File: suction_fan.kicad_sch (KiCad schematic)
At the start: 4 parts, among them U5_1 DRV8835DSSR

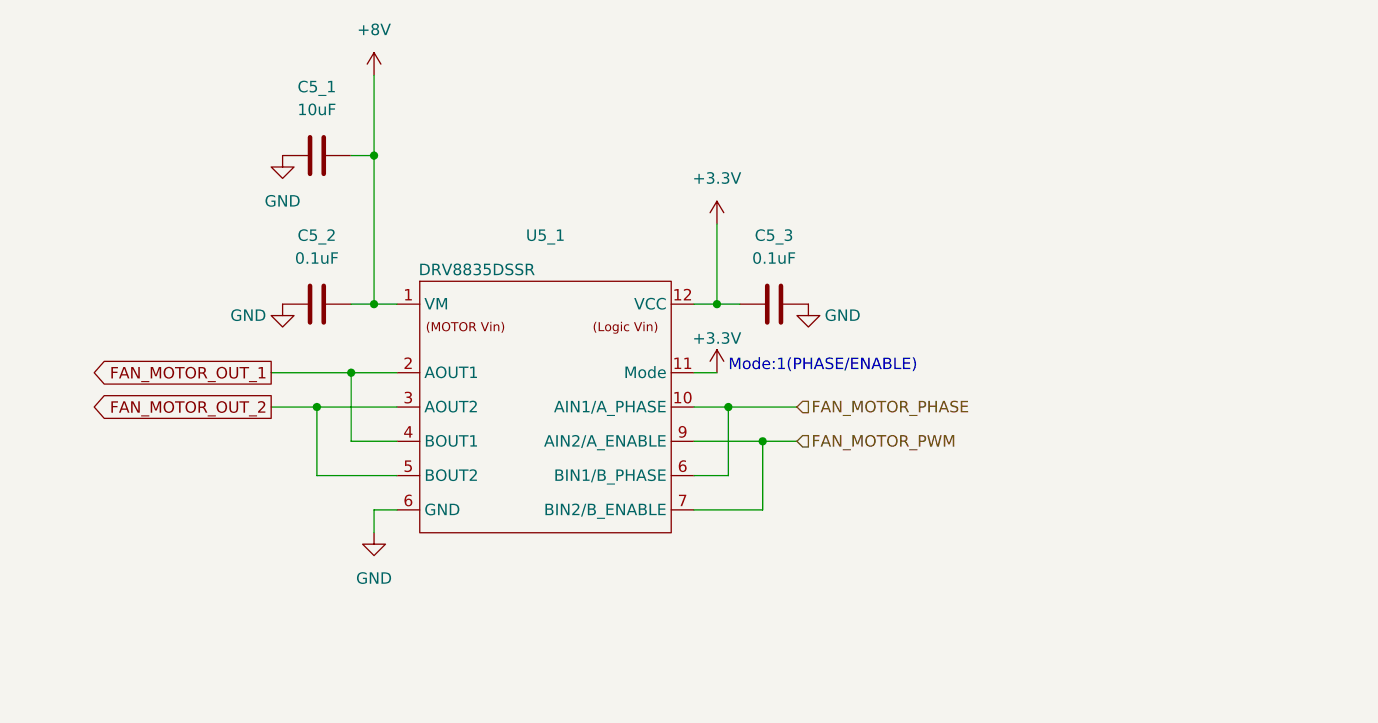
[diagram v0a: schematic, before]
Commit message: 吸引ファンモータのコネクタを追加
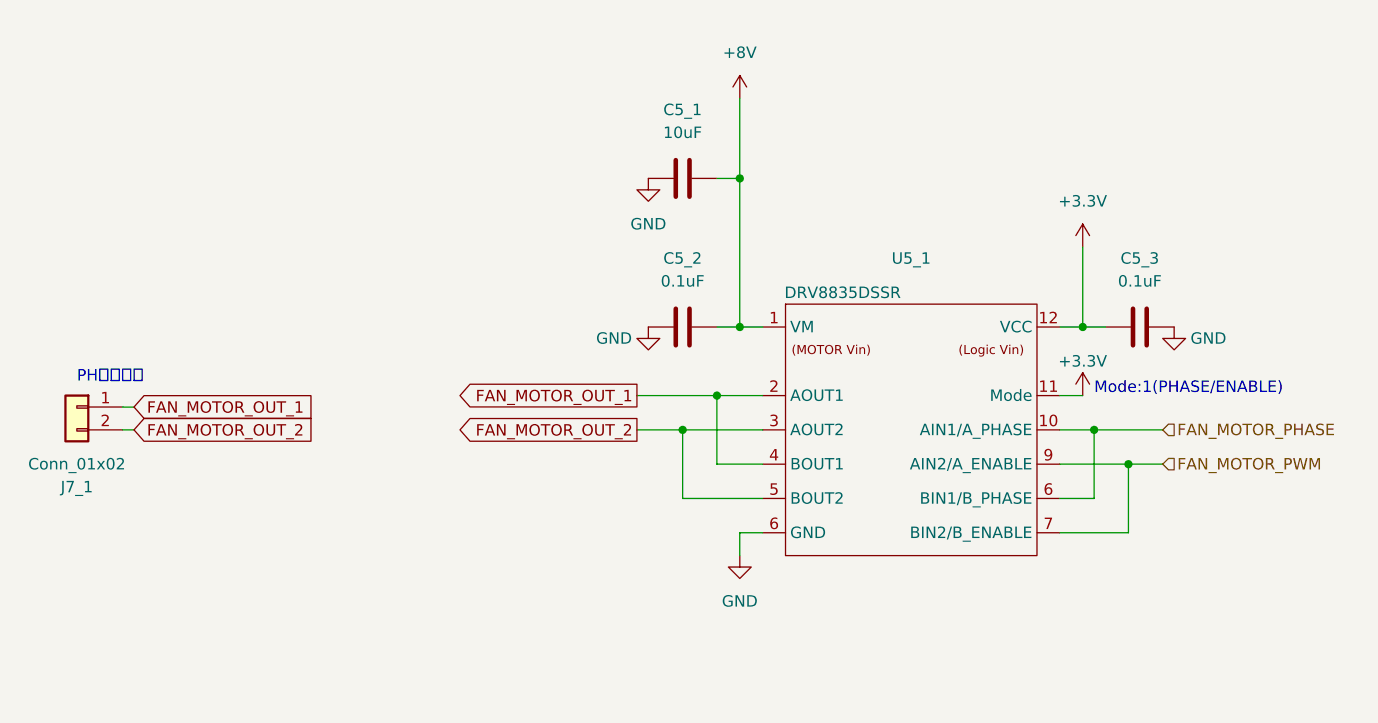
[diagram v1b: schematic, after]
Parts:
- added J7_1: Conn_01x02, symbol Connector_Generic:Conn_01x02
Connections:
- net FAN_MOTOR_OUT_1: now also J7_1.1 (Pin_1)
- net FAN_MOTOR_OUT_2: now also J7_1.2 (Pin_2)
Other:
- note added: "PHコネクタ"
- moved on the sheet: C5_1, C5_2, C5_3, U5_1

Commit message: 吸引モータ周りの回路修正
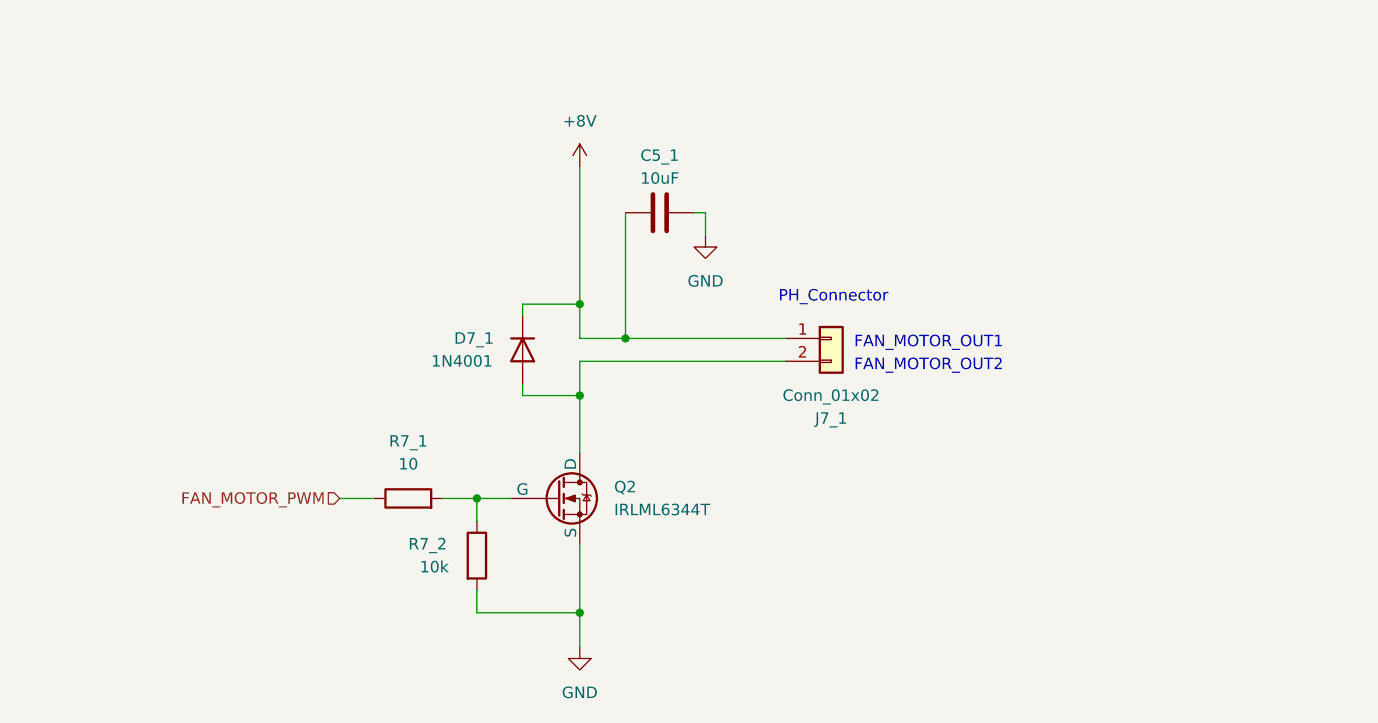
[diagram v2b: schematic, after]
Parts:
- removed C5_2, C5_3: 0.1uF, Capacitor_SMD:C_0603_1608Metric_Pad1.08x0.95mm_HandSolder, symbol Device:C
- removed U5_1: DRV8835DSSR, Self-Made_Generic_Packages:WSON-12-1EP_ExpandPad_3x2mm_P0.5mm_EP1x2.65, symbol DRV8835:DRV8835
- added D7_1: 1N4001, Diode_THT:D_DO-41_SOD81_P10.16mm_Horizontal, symbol Diode:1N4001
- added Q2: IRLML6344T, Package_TO_SOT_SMD:SOT-23, symbol Simulation_SPICE:NMOS
- added R7_1: 10, symbol Device:R
- added R7_2: 10k, symbol Device:R
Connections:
- net FAN_MOTOR_OUT_1 is gone; now on net +8V: J7_1.1 (Pin_1)
- net +8V: now also C5_1.1, D7_1.1 (K); no longer C5_1.2
- net FAN_MOTOR_PWM: now also R7_1.1
- net GND: now also C5_1.2, Q2.3 (S), R7_2.2; no longer C5_1.1
- net FAN_MOTOR_OUT_2: no longer names the net of J7_1.2 (Pin_2)
- net FAN_MOTOR_OUT_2: now also D7_1.2 (A), Q2.1 (D)
- new net: Q2.2 (G), R7_1.2, R7_2.1
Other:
- note added: "FAN_MOTOR_OUT1"
- note added: "FAN_MOTOR_OUT2"
- note added: "PH_Connector"
- note removed: "Mode:1(PHASE/ENABLE)"
- note removed: "PHコネクタ"
- moved on the sheet: C5_1, J7_1

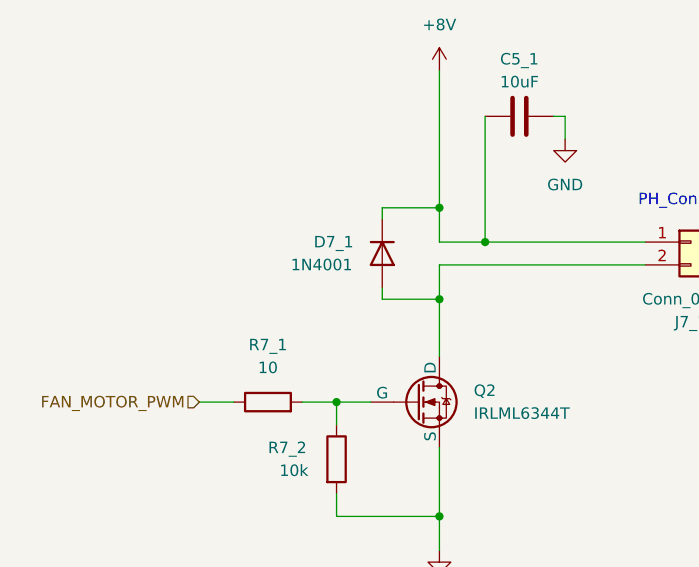
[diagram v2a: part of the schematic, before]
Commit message: 吸引ファンのダイオードの規格やフットプリント割当を完了（完成）
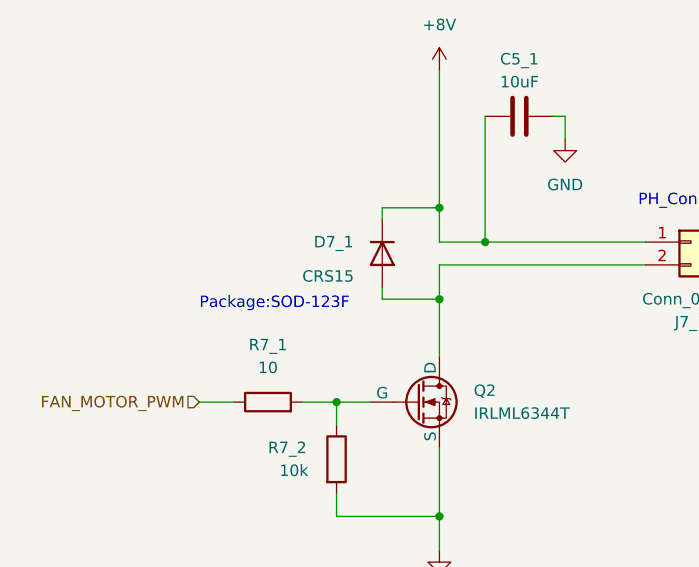
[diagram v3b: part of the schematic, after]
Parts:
- D7_1: value 1N4001 -> CRS15; footprint Diode_THT:D_DO-41_SOD81_P10.16mm_Horizontal -> Diode_SMD:D_SOD-123F
- J7_1: footprint (none) -> Connector_JST:JST_PH_B2B-PH-K_1x02_P2.00mm_Vertical
- R7_1, R7_2: footprint (none) -> Resistor_SMD:R_0603_1608Metric_Pad0.98x0.95mm_HandSolder
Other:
- note added: "Package:SOD-123F"
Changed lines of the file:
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@@
     (effects (font (size 1.27 1.27)) (justify right bottom))
+  )
+  (text "Package:SOD-123F" (at 120.65 105.41 0)
+    (effects (font (size 1.27 1.27)) (justify left bottom))
   )
   (hierarchical_label "FAN_MOTOR_PWM" (shape input) (at 120.65 115.57 180) (fields_autoplaced)
@@
       (effects (font (size 1.27 1.27)) (justify left))
     )
-    (property "Footprint" "" (at 134.112 121.92 90)
+    (property "Footprint" "Resistor_SMD:R_0603_1608Metric_Pad0.98x0.95mm_HandSolder" (at 134.112 121.92 90)
       (effects (font (size 1.27 1.27)) hide)
     )
@@
       (effects (font (size 1.27 1.27)))
     )
-    (property "Footprint" "" (at 175.26 97.79 0)
+    (property "Footprint" "Connector_JST:JST_PH_B2B-PH-K_1x02_P2.00mm_Vertical" (at 175.26 97.79 0)
       (effects (font (size 1.27 1.27)) hide)
     )
@@
       (effects (font (size 1.27 1.27)))
     )
-    (property "Footprint" "" (at 128.27 117.348 90)
+    (property "Footprint" "Resistor_SMD:R_0603_1608Metric_Pad0.98x0.95mm_HandSolder" (at 128.27 117.348 90)
       (effects (font (size 1.27 1.27)) hide)
     )
@@
       (effects (font (size 1.27 1.27)) (justify left))
     )
-    (property "Value" "1N4001" (at 130.81 100.33 90)
-      (effects (font (size 1.27 1.27)) (justify left))
-    )
-    (property "Footprint" "Diode_THT:D_DO-41_SOD81_P10.16mm_Horizontal" (at 140.97 99.06 0)
-      (effects (font (size 1.27 1.27)) hide)
-    )
+    (property "Value" "CRS15" (at 132.08 101.6 90)
+      (effects (font (size 1.27 1.27)) (justify left))
+    )
+    (property "Footprint" "Diode_SMD:D_SOD-123F" (at 140.97 99.06 0)
+      (effects (font (size 1.27 1.27)) hide)
+    )

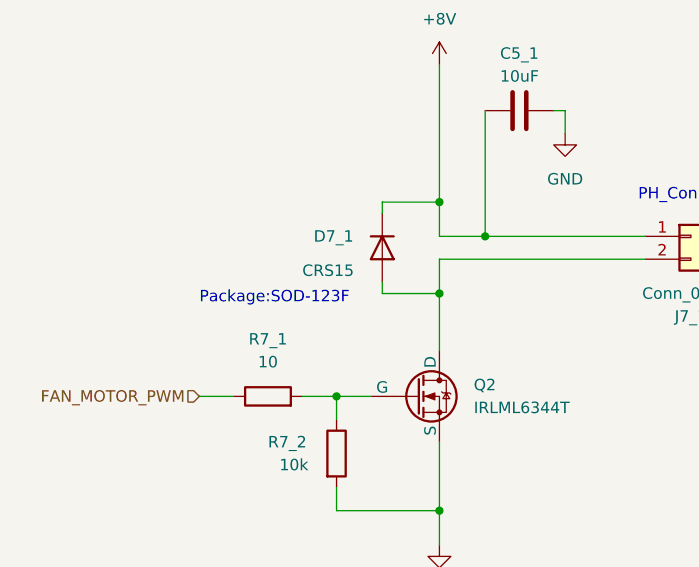
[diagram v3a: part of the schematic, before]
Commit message: AON7421のフットプリント追加
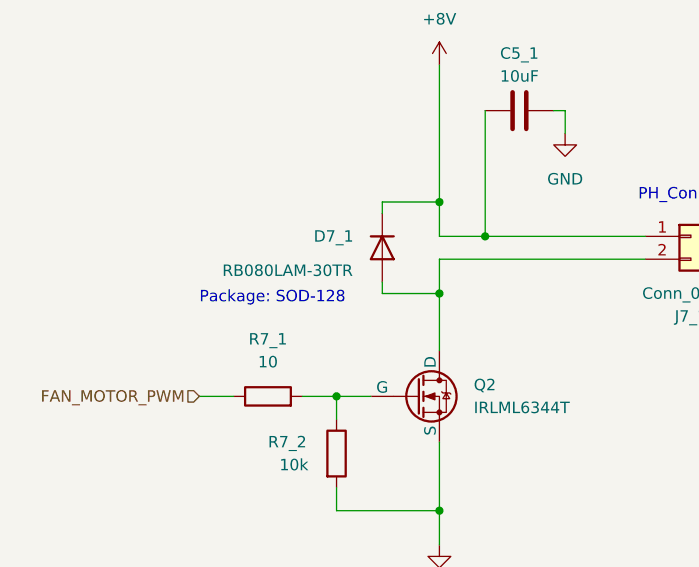
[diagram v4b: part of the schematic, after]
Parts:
- D7_1: value CRS15 -> RB080LAM-30TR; footprint Diode_SMD:D_SOD-123F -> Diode_SMD:D_SOD-128
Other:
- note added: "Package: SOD-128"
- note removed: "Package:SOD-123F"
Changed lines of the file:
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@@
     (effects (font (size 1.27 1.27)) (justify right bottom))
   )
-  (text "Package:SOD-123F" (at 120.65 105.41 0)
+  (text "Package: SOD-128" (at 120.65 105.41 0)
     (effects (font (size 1.27 1.27)) (justify left bottom))
   )
@@
       (effects (font (size 1.27 1.27)) (justify left))
     )
-    (property "Value" "CRS15" (at 132.08 101.6 90)
-      (effects (font (size 1.27 1.27)) (justify left))
-    )
-    (property "Footprint" "Diode_SMD:D_SOD-123F" (at 140.97 99.06 0)
-      (effects (font (size 1.27 1.27)) hide)
-    )
+    (property "Value" "RB080LAM-30TR" (at 123.19 101.6 90)
+      (effects (font (size 1.27 1.27)) (justify left))
+    )
+    (property "Footprint" "Diode_SMD:D_SOD-128" (at 140.97 99.06 0)
+      (effects (font (size 1.27 1.27)) hide)
+    )
